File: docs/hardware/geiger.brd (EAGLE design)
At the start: 100 x 31.9 mm, 33 parts, among them U2 WIFI-32NO_TEXT, U4 BSP125

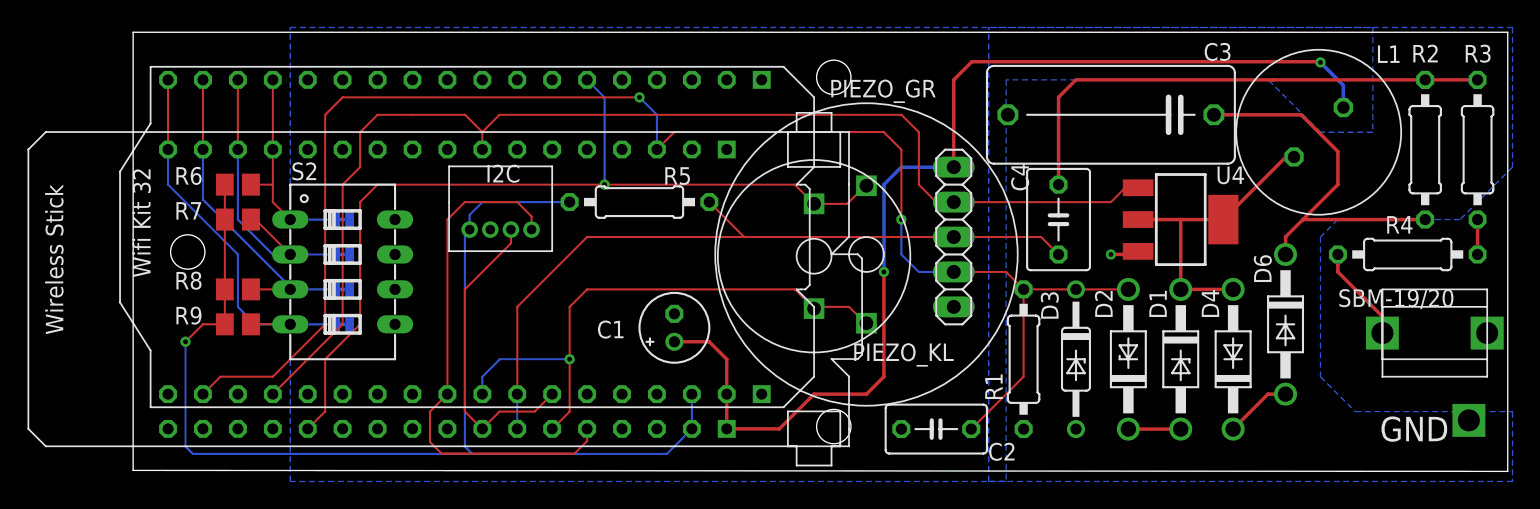
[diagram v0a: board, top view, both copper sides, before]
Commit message: Switch numbering left to right
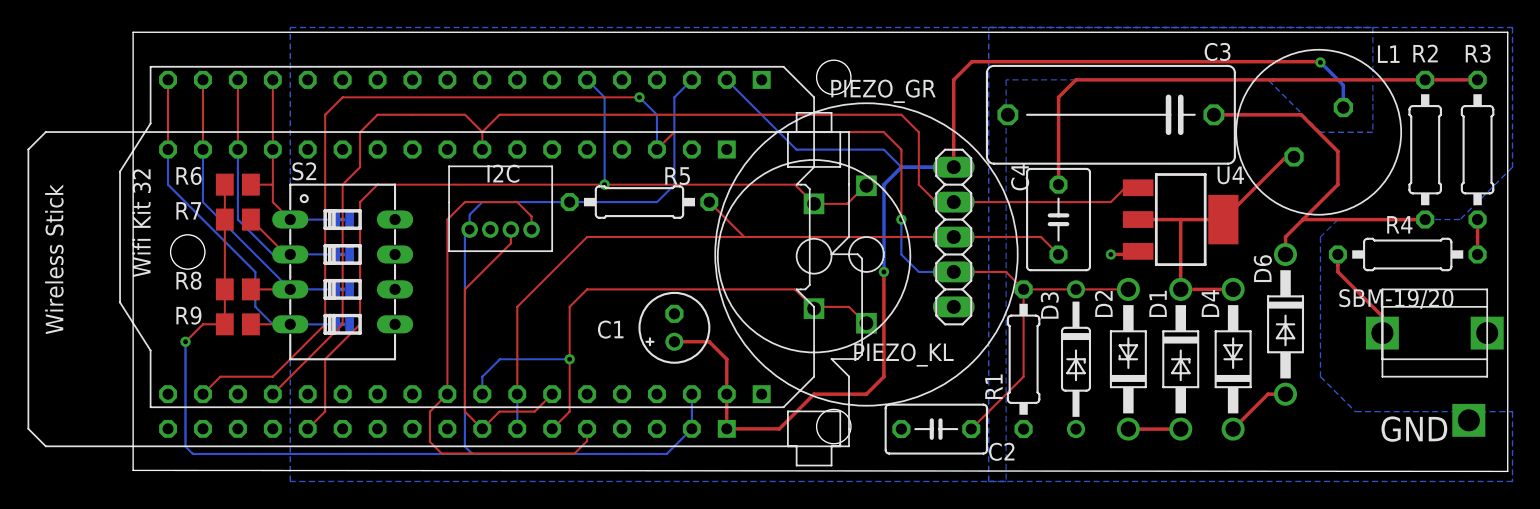
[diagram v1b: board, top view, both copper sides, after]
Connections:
- removed net 3V3: I2C.1, R5.2, R6.2, R7.2, R8.2, R9.2, U$3.P$33, U2.P$34
- removed net 5V: C1.+, JP1.1, L1.1, U$3.P$34, U2.P$35
- removed net SW0: JP5.2, R6.1, S2.1, U$3.P$14, U2.P$15
- new net 3V3@1: I2C.1, R5.2, R6.2, R7.2, R8.2, R9.2, U$3.P$33, U2.P$3, U2.P$34
- new net 5V@1: C1.+, JP1.1, L1.1, U$3.P$34, U2.P$2, U2.P$35
- new net SW4: JP2.2, R9.1, S2.4, U$3.P$17, U2.P$18
- net SW1: now also JP5.2, R6.1, S2.1, U$3.P$14, U2.P$15; no longer JP4.2, R7.1, S2.2, U$3.P$15, U2.P$16
- net SW2: now also JP4.2, R7.1, S2.2, U$3.P$15, U2.P$16; no longer JP3.2, R8.1, S2.3, U$3.P$16, U2.P$17
- net SW3: now also JP3.2, R8.1, S2.3, U$3.P$16, U2.P$17; no longer JP2.2, R9.1, S2.4, U$3.P$17, U2.P$18
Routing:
- net 3V3@1: track 0.00 -> 103.2 mm, vias 0 -> 1
- net 5V@1: track 0.00 -> 94.9 mm, vias 0 -> 2
- net 3V3: track 86.9 -> 0.00 mm, vias 1 -> 0
- net 5V: track 79.5 -> 0.00 mm, vias 2 -> 0
- net SW4: track 0.00 -> 28.4 mm
- net SW0: track 15.6 -> 0.00 mm
- net SW1: track 22.2 -> 15.6 mm
- net SW3: track 29.1 -> 24.0 mm
- net SW2: track 24.0 -> 22.2 mm

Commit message: fixed schematic/layout error with new hardware
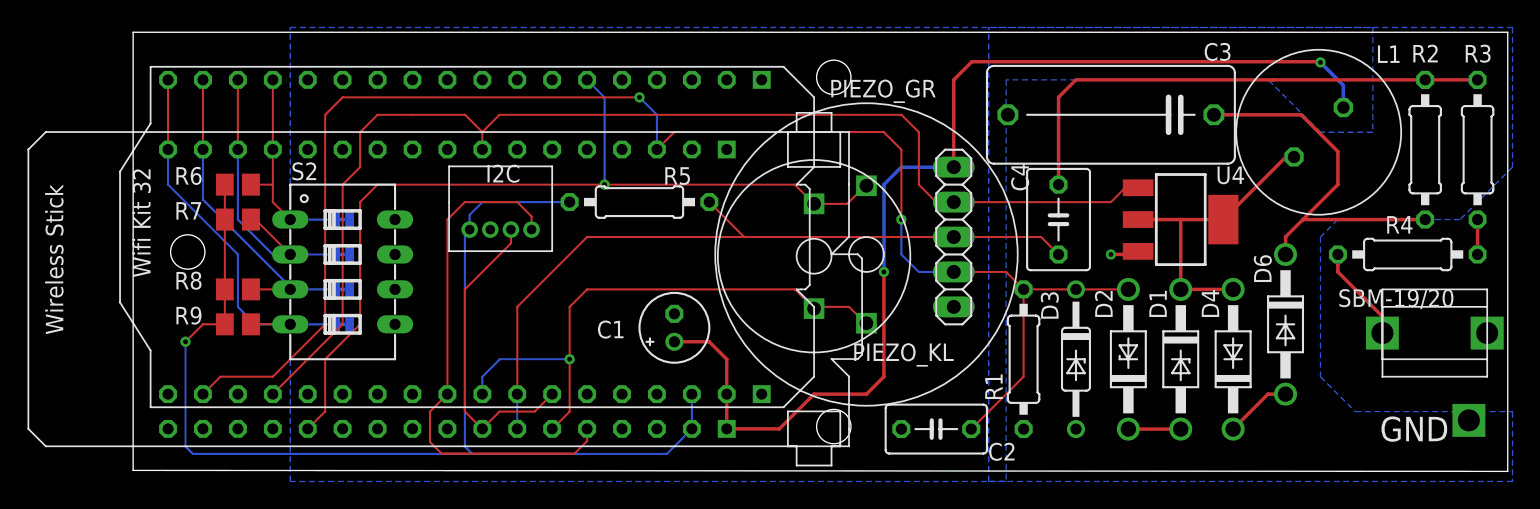
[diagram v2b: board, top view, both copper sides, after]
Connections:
- removed net 3V3@1: I2C.1, R5.2, R6.2, R7.2, R8.2, R9.2, U$3.P$33, U2.P$3, U2.P$34
- removed net 5V@1: C1.+, JP1.1, L1.1, U$3.P$34, U2.P$2, U2.P$35
- removed net SW4: JP2.2, R9.1, S2.4, U$3.P$17, U2.P$18
- new net 3V3: I2C.1, R5.2, R6.2, R7.2, R8.2, R9.2, U$3.P$33, U2.P$34
- new net 5V: C1.+, JP1.1, L1.1, U$3.P$34, U2.P$35
- new net SW0: JP5.2, R6.1, S2.1, U$3.P$14, U2.P$15
- net SW1: now also JP4.2, R7.1, S2.2, U$3.P$15, U2.P$16; no longer JP5.2, R6.1, S2.1, U$3.P$14, U2.P$15
- net SW2: now also JP3.2, R8.1, S2.3, U$3.P$16, U2.P$17; no longer JP4.2, R7.1, S2.2, U$3.P$15, U2.P$16
- net SW3: now also JP2.2, R9.1, S2.4, U$3.P$17, U2.P$18; no longer JP3.2, R8.1, S2.3, U$3.P$16, U2.P$17
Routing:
- net 3V3@1: track 103.2 -> 0.00 mm, vias 1 -> 0
- net 5V@1: track 94.9 -> 0.00 mm, vias 2 -> 0
- net 3V3: track 0.00 -> 86.9 mm, vias 0 -> 1
- net 5V: track 0.00 -> 79.5 mm, vias 0 -> 2
- net SW4: track 28.4 -> 0.00 mm
- net SW0: track 0.00 -> 15.6 mm
- net SW1: track 15.6 -> 22.2 mm
- net SW3: track 24.0 -> 29.1 mm
- net SW2: track 22.2 -> 24.0 mm
